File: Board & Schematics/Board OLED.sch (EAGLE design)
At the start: 21 parts

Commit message: removed cream from bottom ICSP Header
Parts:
- added PWR: (no value), SparkFun-LED:LED0603
- added R10: 91Ω, rcl:R-EU_R0603
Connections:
- new net N$4: PWR.C, R10.2
- net +5V: now also PWR.A
- net GND: now also R10.1
- net MOSI: now also R9.1, U$2.SDA; no longer R8.1, U$2.SCL
- net SCK: now also R8.1, U$2.SCL; no longer R9.1, U$2.SDA
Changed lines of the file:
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@@
 <part name="VI" library="OwnStuff" deviceset="TESTPOINT" device="0.5MM-DRILL-WIRE-LOOP"/>
 <part name="VO" library="OwnStuff" deviceset="TESTPOINT" device="0.5MM-DRILL-WIRE-LOOP"/>
+<part name="P+6" library="supply1" deviceset="+5V" device=""/>
+<part name="GND7" library="SparkFun-Aesthetics" deviceset="GND" device=""/>
+<part name="PWR" library="SparkFun-LED" deviceset="LED" device="0603"/>
+<part name="R10" library="rcl" deviceset="R-EU_" device="R0603" value="91Ω"/>
 </parts>
 <sheets>
@@
 <instance part="VI" gate="G$1" x="20.32" y="58.42"/>
 <instance part="VO" gate="G$1" x="40.64" y="58.42"/>
+<instance part="P+6" gate="1" x="116.84" y="5.08"/>
+<instance part="GND7" gate="1" x="116.84" y="-17.78"/>
+<instance part="PWR" gate="G$1" x="116.84" y="0"/>
+<instance part="R10" gate="G$1" x="116.84" y="-10.16" rot="R90"/>
 </instances>
 <busses>
@@
 <junction x="66.04" y="50.8"/>
 </segment>
+<segment>
+<pinref part="R10" gate="G$1" pin="1"/>
+<pinref part="GND7" gate="1" pin="GND"/>
+</segment>
 </net>
 <net name="+5V" class="0">
@@
 <wire x1="30.48" y1="60.96" x2="30.48" y2="58.42" width="0.1524" layer="91"/>
 </segment>
+<segment>
+<pinref part="P+6" gate="1" pin="+5V"/>
+<pinref part="PWR" gate="G$1" pin="A"/>
+</segment>
 </net>
 <net name="RST" class="0">
@@
 <wire x1="48.26" y1="0" x2="35.56" y2="0" width="0.1524" layer="91"/>
 <wire x1="48.26" y1="0" x2="48.26" y2="15.24" width="0.1524" layer="91"/>
-<wire x1="88.9" y1="2.54" x2="83.82" y2="2.54" width="0.1524" layer="91"/>
-<wire x1="83.82" y1="2.54" x2="73.66" y2="2.54" width="0.1524" layer="91"/>
-<wire x1="73.66" y1="2.54" x2="73.66" y2="15.24" width="0.1524" layer="91"/>
-<wire x1="73.66" y1="15.24" x2="48.26" y2="15.24" width="0.1524" layer="91"/>
+<wire x1="76.2" y1="-2.54" x2="76.2" y2="15.24" width="0.1524" layer="91"/>
+<wire x1="76.2" y1="15.24" x2="48.26" y2="15.24" width="0.1524" layer="91"/>
 <label x="50.8" y="15.24" size="1.778" layer="95" rot="R90" xref="yes"/>
-<pinref part="U$2" gate="G$1" pin="SCL"/>
-<pinref part="R8" gate="G$1" pin="1"/>
-<junction x="83.82" y="2.54"/>
+<pinref part="U$2" gate="G$1" pin="SDA"/>
+<wire x1="86.36" y1="-2.54" x2="88.9" y2="-2.54" width="0.1524" layer="91"/>
+<pinref part="R9" gate="G$1" pin="1"/>
+<wire x1="76.2" y1="-2.54" x2="86.36" y2="-2.54" width="0.1524" layer="91"/>
+<junction x="86.36" y="-2.54"/>
 </segment>
 <segment>
@@
 <segment>
 <wire x1="58.42" y1="-10.16" x2="78.74" y2="-10.16" width="0.1524" layer="91"/>
-<wire x1="78.74" y1="-10.16" x2="78.74" y2="-2.54" width="0.1524" layer="91"/>
-<wire x1="78.74" y1="-2.54" x2="86.36" y2="-2.54" width="0.1524" layer="91"/>
+<wire x1="78.74" y1="-10.16" x2="78.74" y2="2.54" width="0.1524" layer="91"/>
 <label x="58.42" y="-7.62" size="1.778" layer="95" xref="yes"/>
 <pinref part="ATTINY85" gate="G$1" pin="PB2(SCK/ADC1)"/>
-<wire x1="86.36" y1="-2.54" x2="88.9" y2="-2.54" width="0.1524" layer="91"/>
 <wire x1="35.56" y1="-5.08" x2="58.42" y2="-5.08" width="0.1524" layer="91"/>
 <wire x1="58.42" y1="-10.16" x2="58.42" y2="-5.08" width="0.1524" layer="91"/>
-<pinref part="U$2" gate="G$1" pin="SDA"/>
-<pinref part="R9" gate="G$1" pin="1"/>
-<junction x="86.36" y="-2.54"/>
+<pinref part="U$2" gate="G$1" pin="SCL"/>
+<wire x1="88.9" y1="2.54" x2="83.82" y2="2.54" width="0.1524" layer="91"/>
+<pinref part="R8" gate="G$1" pin="1"/>
+<wire x1="78.74" y1="2.54" x2="83.82" y2="2.54" width="0.1524" layer="91"/>
+<junction x="83.82" y="2.54"/>
 </segment>
 <segment>
@@
 </segment>
 </net>
+<net name="N$4" class="0">
+<segment>
+<pinref part="PWR" gate="G$1" pin="C"/>
+<pinref part="R10" gate="G$1" pin="2"/>
+</segment>
+</net>

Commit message: fixed silkscreen and schematic designator for new, smaller shunt
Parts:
- R1: value 1Ω -> 0.1Ω
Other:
- note added: "ISense = 1V @6V Input, ISense max = 6.6V I @ 1/6V Drop = 0.1A"
- note removed: "ISense = 1V @6V Input, ISense max = 6.6V I @ 1/6V Drop = 1A"
- note removed: "using internal 1.1V reference: max measured output = 1A nearest value = 1ohm: actual max I=1.1A"
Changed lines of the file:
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@@
 <parts>
 <part name="INPUT" library="SparkFun-Connectors" deviceset="USB+SHIELD" device="THROUGHHOLE-MALE" value="USB+SHIELDTHROUGHHOLE-MALE"/>
-<part name="R1" library="rcl" deviceset="R-EU_" device="R2512" value="1Ω"/>
+<part name="R1" library="rcl" deviceset="R-EU_" device="R2512" value="0.1Ω"/>
 <part name="GND1" library="SparkFun-Aesthetics" deviceset="GND" device=""/>
 <part name="P+1" library="supply1" deviceset="+5V" device=""/>
@@
 <sheet>
 <plain>
-<text x="15.24" y="71.12" size="1.778" layer="91">using internal 1.1V reference:
-max measured output = 1A
-nearest value = 1ohm: actual max I=1.1A</text>
 <text x="0" y="33.02" size="1.778" layer="91">VSense = 1V @6V Input,
 VSense max = 6.6V</text>
 <text x="48.26" y="33.02" size="1.778" layer="91">ISense = 1V @6V Input,
 ISense max = 6.6V
-I @ 1/6V Drop = 1A</text>
+I @ 1/6V Drop = 0.1A</text>
 </plain>
 <instances>

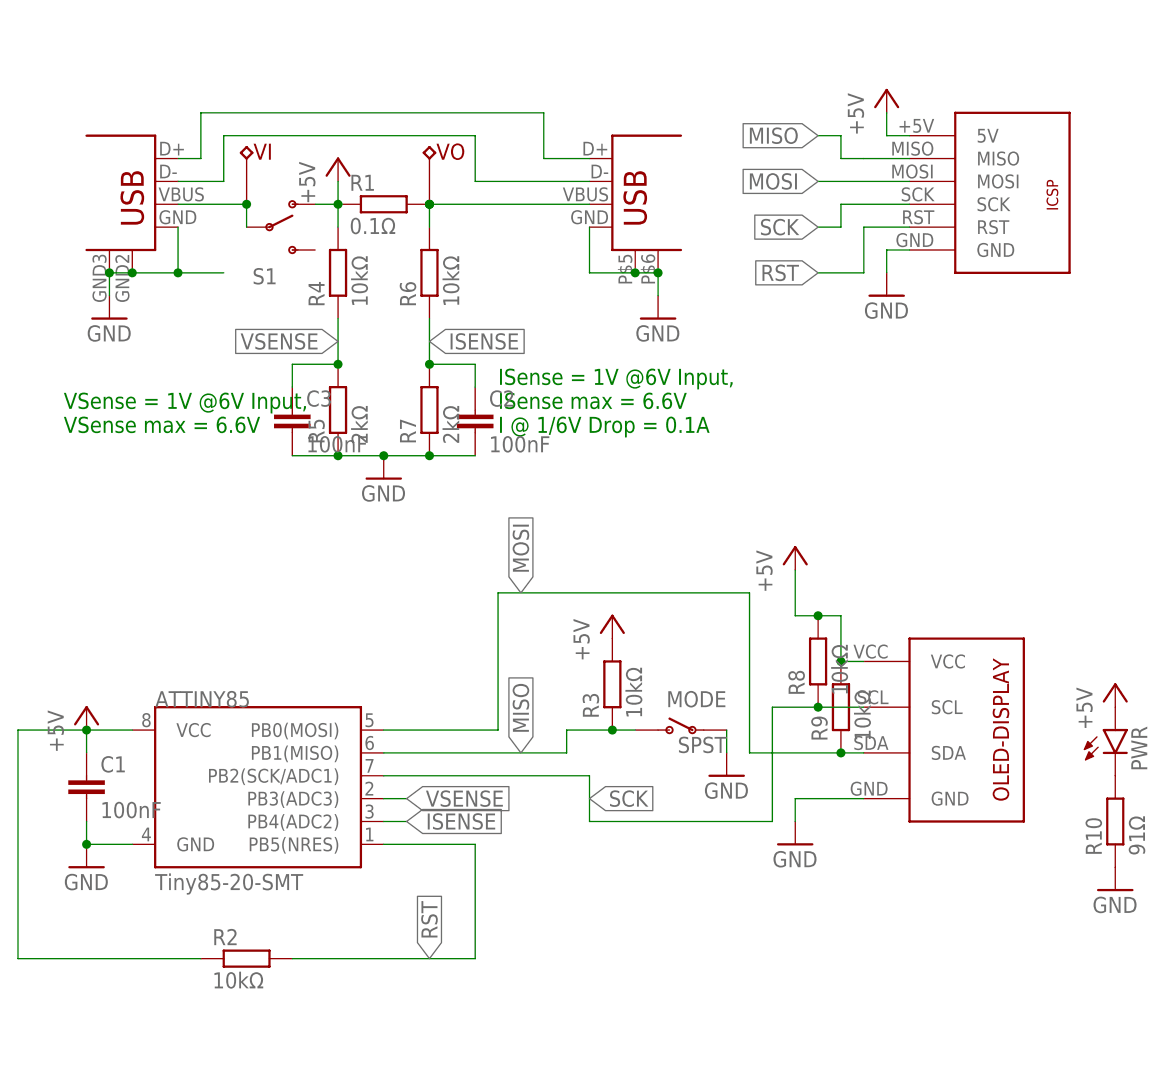
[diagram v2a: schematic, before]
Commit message: remove attenuation from OLED variant
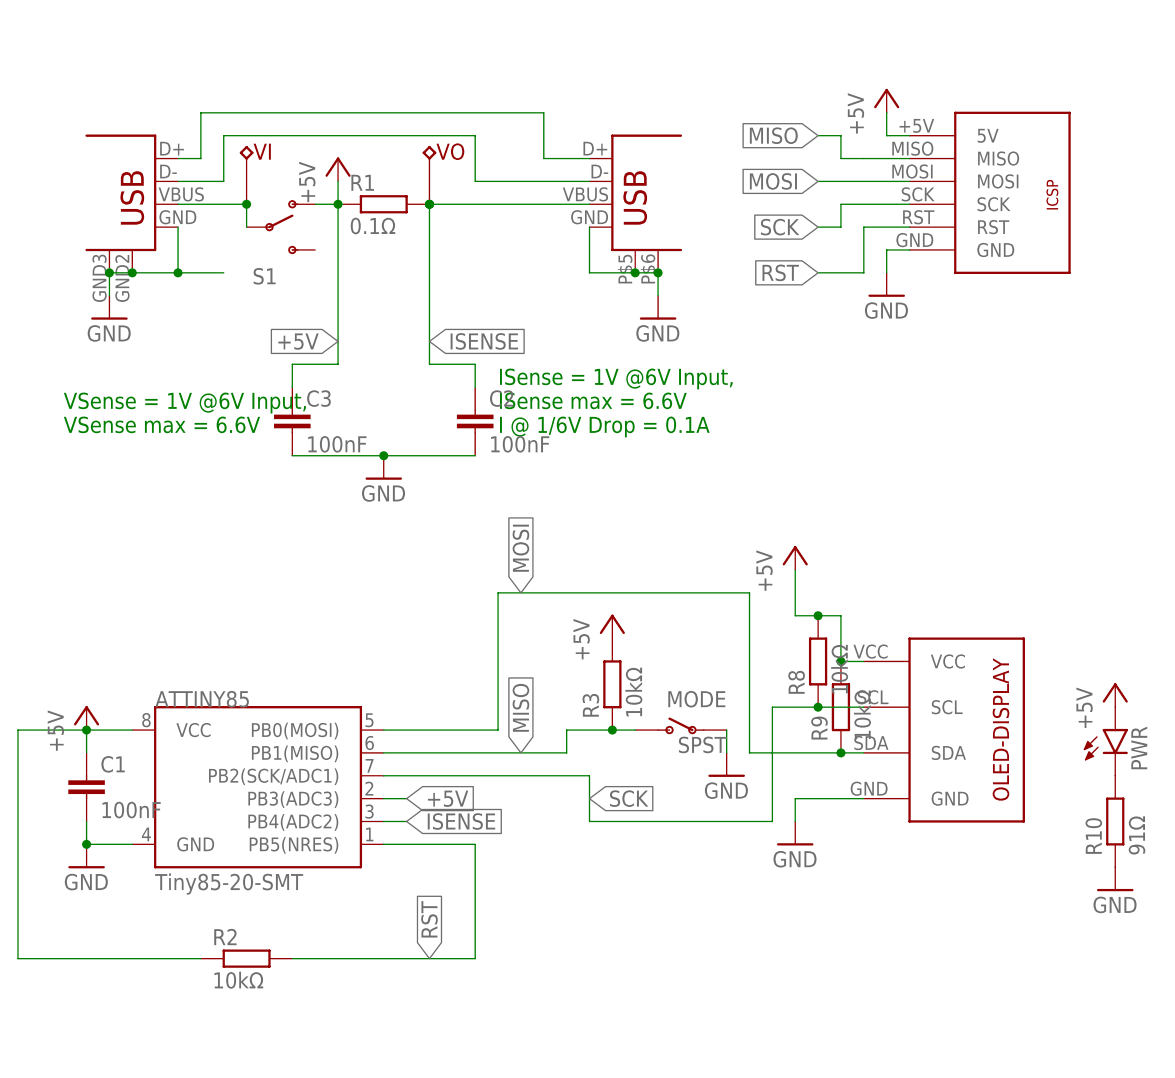
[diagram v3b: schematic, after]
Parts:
- removed R4, R6: 10kΩ, rcl:R-EU_R0603
- removed R5, R7: 2kΩ, rcl:R-EU_R0603
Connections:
- removed net N$6: OUTPUT.VBUS, R1.2, R6.2, VO.TP
- removed net VSENSE: ATTINY85.PB3(ADC3), C3.1, R4.1, R5.2
- net +5V: now also ATTINY85.PB3(ADC3), C3.1; no longer R4.2
- net GND: no longer R5.1, R7.1
- net ISENSE: now also OUTPUT.VBUS, R1.2, VO.TP; no longer R6.1, R7.2
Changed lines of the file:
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@@
 <part name="P+5" library="supply1" deviceset="+5V" device=""/>
 <part name="GND6" library="SparkFun-Aesthetics" deviceset="GND" device=""/>
-<part name="R4" library="rcl" deviceset="R-EU_" device="R0603" value="10kΩ"/>
-<part name="R5" library="rcl" deviceset="R-EU_" device="R0603" value="2kΩ"/>
-<part name="R6" library="rcl" deviceset="R-EU_" device="R0603" value="10kΩ"/>
-<part name="R7" library="rcl" deviceset="R-EU_" device="R0603" value="2kΩ"/>
 <part name="GND8" library="SparkFun-Aesthetics" deviceset="GND" device=""/>
 <part name="S1" library="SparkFun-Electromechanical" deviceset="SWITCH-SPDT" device="-SMD-A"/>
@@
 <instance part="P+5" gate="1" x="91.44" y="71.12"/>
 <instance part="GND6" gate="1" x="91.44" y="48.26"/>
-<instance part="R4" gate="G$1" x="30.48" y="50.8" rot="R90"/>
-<instance part="R5" gate="G$1" x="30.48" y="35.56" rot="R90"/>
-<instance part="R6" gate="G$1" x="40.64" y="50.8" rot="R90"/>
-<instance part="R7" gate="G$1" x="40.64" y="35.56" rot="R90"/>
 <instance part="GND8" gate="1" x="35.56" y="27.94"/>
 <instance part="S1" gate="1" x="22.86" y="55.88"/>
@@
 </segment>
 <segment>
-<pinref part="R5" gate="G$1" pin="1"/>
 <pinref part="GND8" gate="1" pin="GND"/>
-<wire x1="30.48" y1="30.48" x2="35.56" y2="30.48" width="0.1524" layer="91"/>
-<wire x1="35.56" y1="30.48" x2="40.64" y2="30.48" width="0.1524" layer="91"/>
 <junction x="35.56" y="30.48"/>
-<pinref part="R7" gate="G$1" pin="1"/>
 <pinref part="C2" gate="G$1" pin="2"/>
-<wire x1="45.72" y1="30.48" x2="40.64" y2="30.48" width="0.1524" layer="91"/>
-<junction x="40.64" y="30.48"/>
+<wire x1="45.72" y1="30.48" x2="35.56" y2="30.48" width="0.1524" layer="91"/>
 <pinref part="C3" gate="G$1" pin="2"/>
-<wire x1="25.4" y1="30.48" x2="30.48" y2="30.48" width="0.1524" layer="91"/>
-<junction x="30.48" y="30.48"/>
+<wire x1="25.4" y1="30.48" x2="35.56" y2="30.48" width="0.1524" layer="91"/>
 </segment>
 <segment>
@@
 <pinref part="S1" gate="1" pin="O"/>
 <pinref part="R1" gate="G$1" pin="1"/>
-<pinref part="R4" gate="G$1" pin="2"/>
-<wire x1="30.48" y1="55.88" x2="30.48" y2="58.42" width="0.1524" layer="91"/>
 <wire x1="27.94" y1="58.42" x2="30.48" y2="58.42" width="0.1524" layer="91"/>
 <junction x="30.48" y="58.42"/>
 <pinref part="P+1" gate="1" pin="+5V"/>
 <wire x1="30.48" y1="60.96" x2="30.48" y2="58.42" width="0.1524" layer="91"/>
+<label x="30.48" y="43.18" size="1.778" layer="95" rot="R180" xref="yes"/>
+<pinref part="C3" gate="G$1" pin="1"/>
+<wire x1="30.48" y1="40.64" x2="25.4" y2="40.64" width="0.1524" layer="91"/>
+<wire x1="25.4" y1="40.64" x2="25.4" y2="38.1" width="0.1524" layer="91"/>
+<wire x1="30.48" y1="58.42" x2="30.48" y2="40.64" width="0.1524" layer="91"/>
 </segment>
 <segment>
 <pinref part="P+6" gate="1" pin="+5V"/>
 <pinref part="PWR" gate="G$1" pin="A"/>
+</segment>
+<segment>
+<pinref part="ATTINY85" gate="G$1" pin="PB3(ADC3)"/>
+<wire x1="35.56" y1="-7.62" x2="38.1" y2="-7.62" width="0.1524" layer="91"/>
+<label x="38.1" y="-7.62" size="1.778" layer="95" xref="yes"/>
 </segment>
 </net>
@@
 <wire x1="88.9" y1="50.8" x2="83.82" y2="50.8" width="0.1524" layer="91"/>
 <label x="83.82" y="50.8" size="1.778" layer="95" rot="R180" xref="yes"/>
-</segment>
-</net>
-<net name="N$6" class="0">
-<segment>
-<pinref part="R1" gate="G$1" pin="2"/>
-<pinref part="OUTPUT" gate="G$1" pin="VBUS"/>
-<junction x="40.64" y="58.42"/>
-<pinref part="R6" gate="G$1" pin="2"/>
-<wire x1="40.64" y1="58.42" x2="58.42" y2="58.42" width="0.1524" layer="91"/>
-<wire x1="40.64" y1="55.88" x2="40.64" y2="58.42" width="0.1524" layer="91"/>
-<junction x="40.64" y="58.42"/>
-<pinref part="VO" gate="G$1" pin="TP"/>
 </segment>
 </net>
@@
 </segment>
 </net>
-<net name="VSENSE" class="0">
-<segment>
-<pinref part="ATTINY85" gate="G$1" pin="PB3(ADC3)"/>
-<wire x1="35.56" y1="-7.62" x2="38.1" y2="-7.62" width="0.1524" layer="91"/>
-<label x="38.1" y="-7.62" size="1.778" layer="95" xref="yes"/>
-</segment>
-<segment>
-<pinref part="R4" gate="G$1" pin="1"/>
-<pinref part="R5" gate="G$1" pin="2"/>
-<wire x1="30.48" y1="45.72" x2="30.48" y2="40.64" width="0.1524" layer="91"/>
-<label x="30.48" y="43.18" size="1.778" layer="95" rot="R180" xref="yes"/>
-<pinref part="C3" gate="G$1" pin="1"/>
-<wire x1="30.48" y1="40.64" x2="25.4" y2="40.64" width="0.1524" layer="91"/>
-<wire x1="25.4" y1="40.64" x2="25.4" y2="38.1" width="0.1524" layer="91"/>
-<junction x="30.48" y="40.64"/>
-</segment>
-</net>
 <net name="ISENSE" class="0">
 <segment>
-<pinref part="R6" gate="G$1" pin="1"/>
-<pinref part="R7" gate="G$1" pin="2"/>
-<wire x1="40.64" y1="45.72" x2="40.64" y2="40.64" width="0.1524" layer="91"/>
+<wire x1="40.64" y1="45.72" x2="40.64" y2="43.18" width="0.1524" layer="91"/>
 <label x="40.64" y="43.18" size="1.778" layer="95" xref="yes"/>
 <pinref part="C2" gate="G$1" pin="1"/>
+<wire x1="40.64" y1="43.18" x2="40.64" y2="40.64" width="0.1524" layer="91"/>
 <wire x1="40.64" y1="40.64" x2="45.72" y2="40.64" width="0.1524" layer="91"/>
 <wire x1="45.72" y1="40.64" x2="45.72" y2="38.1" width="0.1524" layer="91"/>
-<junction x="40.64" y="40.64"/>
-</segment>
-<segment>
+<pinref part="R1" gate="G$1" pin="2"/>
+<pinref part="OUTPUT" gate="G$1" pin="VBUS"/>
+<junction x="40.64" y="58.42"/>
+<wire x1="40.64" y1="58.42" x2="58.42" y2="58.42" width="0.1524" layer="91"/>
+<junction x="40.64" y="58.42"/>
+<pinref part="VO" gate="G$1" pin="TP"/>
+<wire x1="40.64" y1="58.42" x2="40.64" y2="45.72" width="0.1524" layer="91"/>
+</segment>
+<segment>

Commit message: switched differential measure polarity
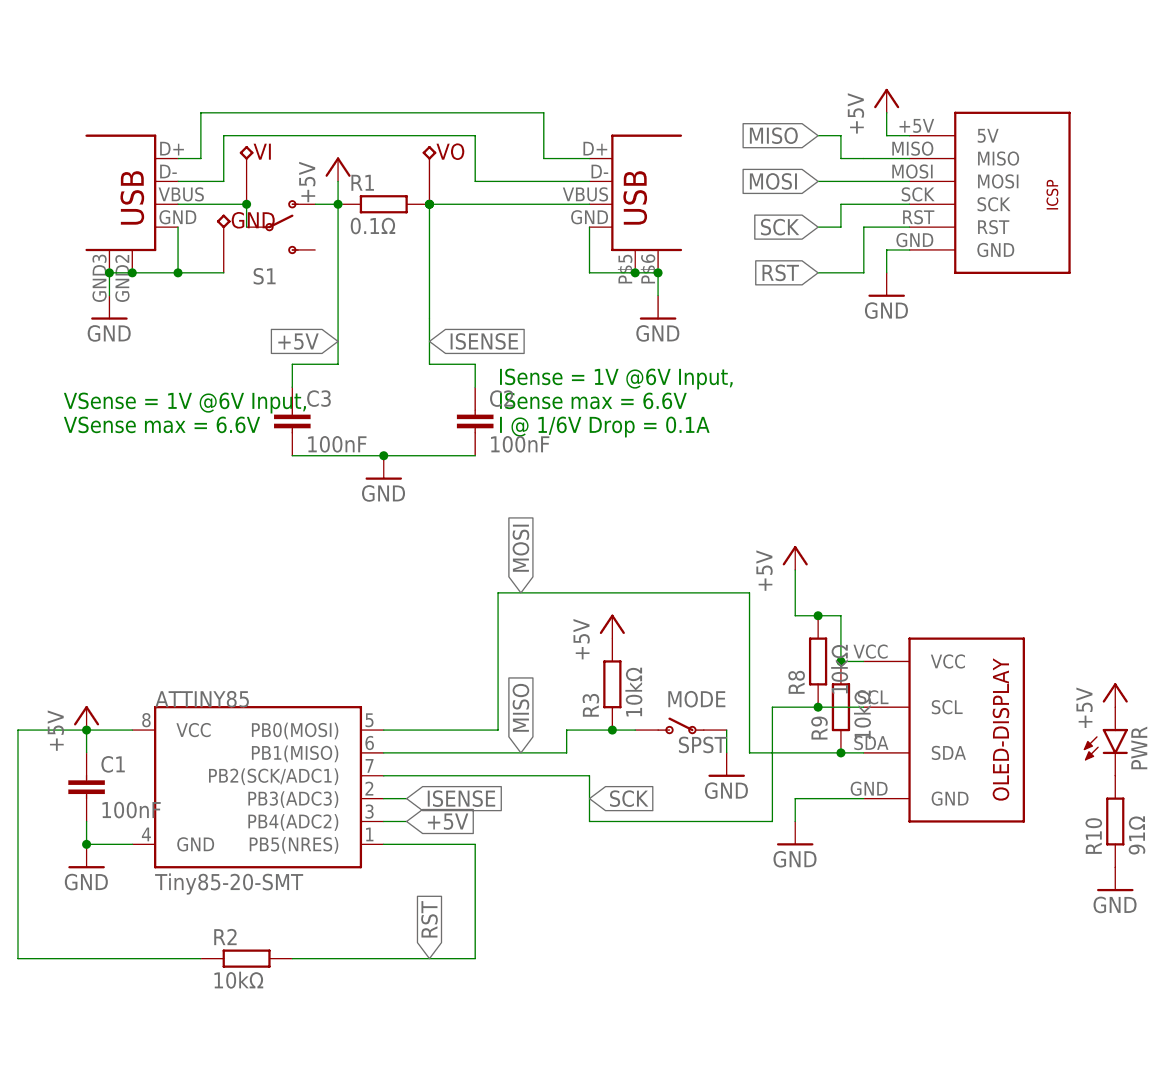
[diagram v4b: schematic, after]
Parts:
- added GND: TESTPOINT0.5MM-DRILL-WIRE-LOOP, OwnStuff:TESTPOINT0.5MM-DRILL-WIRE-LOOP
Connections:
- net +5V: now also ATTINY85.PB4(ADC2); no longer ATTINY85.PB3(ADC3)
- net GND: now also GND.TP
- net ISENSE: now also ATTINY85.PB3(ADC3); no longer ATTINY85.PB4(ADC2)
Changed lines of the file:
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@@
 <part name="PWR" library="SparkFun-LED" deviceset="LED" device="0603"/>
 <part name="R10" library="rcl" deviceset="R-EU_" device="R0603" value="91Ω"/>
+<part name="GND" library="OwnStuff" deviceset="TESTPOINT" device="0.5MM-DRILL-WIRE-LOOP"/>
 </parts>
 <sheets>
@@
 <instance part="PWR" gate="G$1" x="116.84" y="0"/>
 <instance part="R10" gate="G$1" x="116.84" y="-10.16" rot="R90"/>
+<instance part="GND" gate="G$1" x="17.78" y="50.8"/>
 </instances>
 <busses>
@@
 <wire x1="5.08" y1="50.8" x2="5.08" y2="48.26" width="0.1524" layer="91"/>
 <junction x="5.08" y="50.8"/>
+<pinref part="GND" gate="G$1" pin="TP"/>
 </segment>
 <segment>
@@
 </segment>
 <segment>
-<pinref part="ATTINY85" gate="G$1" pin="PB3(ADC3)"/>
-<wire x1="35.56" y1="-7.62" x2="38.1" y2="-7.62" width="0.1524" layer="91"/>
-<label x="38.1" y="-7.62" size="1.778" layer="95" xref="yes"/>
+<pinref part="ATTINY85" gate="G$1" pin="PB4(ADC2)"/>
+<wire x1="38.1" y1="-10.16" x2="35.56" y2="-10.16" width="0.1524" layer="91"/>
+<label x="38.1" y="-10.16" size="1.778" layer="95" xref="yes"/>
 </segment>
 </net>
@@
 </segment>
 <segment>
-<pinref part="ATTINY85" gate="G$1" pin="PB4(ADC2)"/>
-<wire x1="38.1" y1="-10.16" x2="35.56" y2="-10.16" width="0.1524" layer="91"/>
-<label x="38.1" y="-10.16" size="1.778" layer="95" xref="yes"/>
-</segment>
-</net>
+<pinref part="ATTINY85" gate="G$1" pin="PB3(ADC3)"/>
+<wire x1="35.56" y1="-7.62" x2="38.1" y2="-7.62" width="0.1524" layer="91"/>
+<label x="38.1" y="-7.62" size="1.778" layer="95" xref="yes"/>
+</segment>
+</net>
